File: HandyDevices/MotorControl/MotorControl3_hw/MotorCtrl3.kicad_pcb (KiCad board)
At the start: 2 copper layers, 90 x 108 mm, 202 parts, among them Q1 USBLC6_2XX, Q2 MMBT2222, Q3 LED_RGB, SW1 BUTTON, SW2 BUTTON, U1 L6470, U2 L6470, U3 L6470, U4 L6470

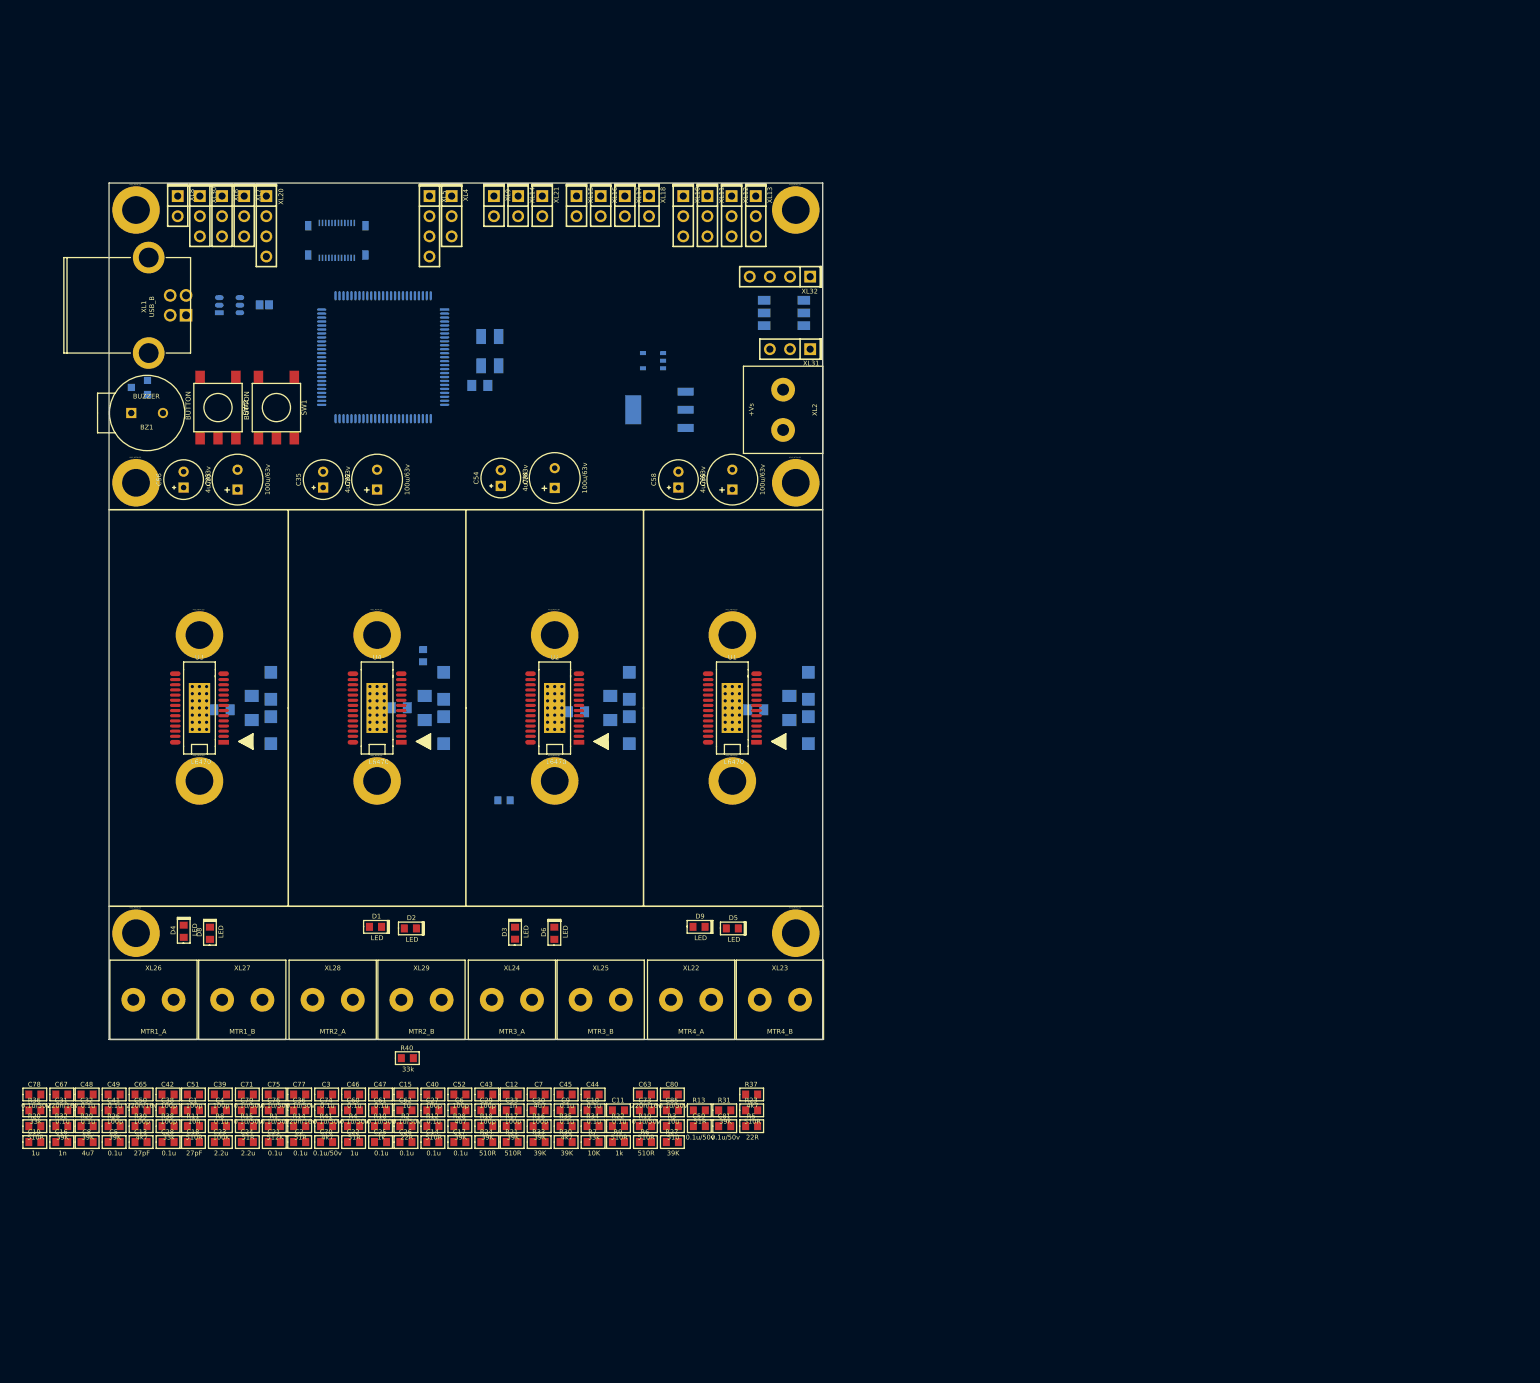
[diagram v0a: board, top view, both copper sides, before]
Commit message: MotorControl3 Footprint aligned.
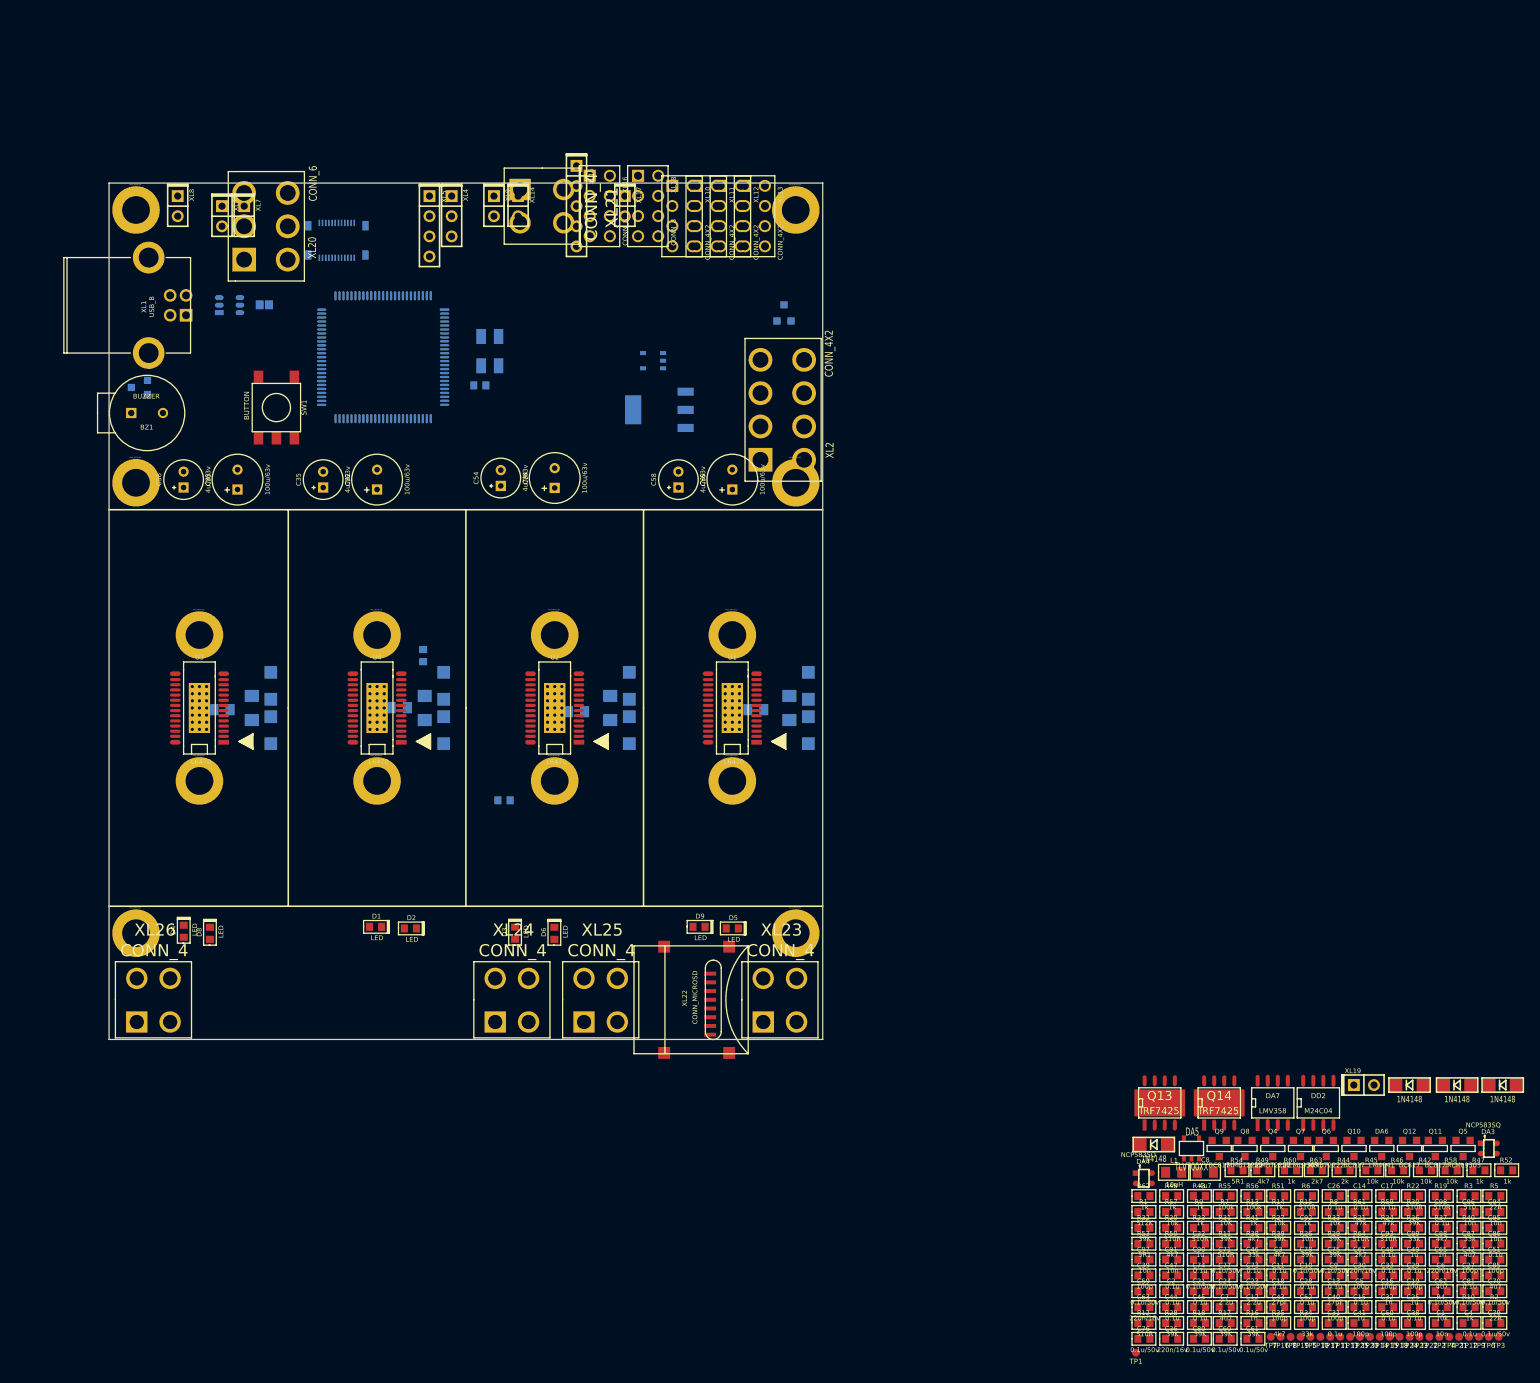
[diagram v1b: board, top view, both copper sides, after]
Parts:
- removed SW2: BUTTON, BUTTON_6x6SMD
- removed XL27: MTR1_B, CONN_KF128D_2
- removed XL28: MTR2_A, CONN_KF128D_2
- removed XL29: MTR2_B, CONN_KF128D_2
- removed XL30, XL31: CONN_3, CONN_PLS-3
- removed XL32: CONN_4, CONN_PLS-4
- added C86: 0.1u, CAP_0603, F.Cu at (350.8, 220.8)
- added C87: 4u7, CAP_0603, F.Cu at (347.5, 220.8)
- added C88: 1n, CAP_0603, F.Cu at (344.0, 220.8)
- added C89: 1u, CAP_0603, F.Cu at (340.5, 220.8)
- added C90: 0.1u, CAP_0603, F.Cu at (313.5, 222.8)
- added C91: 10n, CAP_0603, F.Cu at (310.0, 222.8)
- added C92: 10n, CAP_0603, F.Cu at (327.0, 218.8)
- added C93: 0.1u, CAP_0603, F.Cu at (337.2, 220.8)
- added C94: 10n, CAP_0603, F.Cu at (350.8, 216.8)
- added C95: 10n, CAP_0603, F.Cu at (350.8, 218.8)
- added C96: 10n, CAP_0603, F.Cu at (347.5, 216.8)
- added C97: 10n, CAP_0603, F.Cu at (306.5, 222.8)
- added C98: 0.1u, CAP_0603, F.Cu at (344.0, 216.8)
- added D17: 1N4148, DIODE_SOD80C, F.Cu at (340.0, 200.8)
- added D18: 1N4148, DIODE_SOD80C, F.Cu at (351.8, 200.8)
- added D19: 1N4148, DIODE_SOD80C, F.Cu at (307.8, 208.2)
- added D20: 1N4148, DIODE_SOD80C, F.Cu at (346.0, 200.8)
- added DA3: NCP583SQ, SC82AB, F.Cu at (350.0, 208.8)
- added DA4: NCP583SQ, SC82AB, F.Cu at (306.5, 212.5)
- added DA5: TLV700XX, SOT23-5, F.Cu at (312.5, 208.8)
- added DA6: LM4041, SOT23, F.Cu at (336.5, 208.8)
- added DA7: LMV358, SO8E, F.Cu at (322.8, 203.0)
- added DD2: M24C04, SO8E, F.Cu at (328.5, 203.0)
- added L1: 10uH, IND_0805, F.Cu at (310.2, 211.8)
- added Q10: BC817, SOT23, F.Cu at (333.0, 208.8)
- added Q11: BC817, SOT23, F.Cu at (343.2, 208.8)
- added Q12: BC817, SOT23, F.Cu at (340.0, 208.8)
- added Q13: IRF7425, SO8HEATSINK, F.Cu at (308.5, 203.0)
- added Q14: IRF7425, SO8HEATSINK, F.Cu at (316.0, 203.0)
- added Q4: MMBT2222, SOT23, F.Cu at (322.8, 208.8)
- added Q5: IRLML9303, SOT23, F.Cu at (346.8, 208.8)
- added Q6: MMBT2222, SOT23, F.Cu at (329.5, 208.8)
- added Q7: IRLML9303, SOT23, F.Cu at (326.2, 208.8)
- added Q8: MMBT2222, SOT23, F.Cu at (319.2, 208.8)
- added Q9: BC817, SOT23, F.Cu at (316.0, 208.8)
- added R42: 10k, RES_0603, F.Cu at (342.0, 211.5)
- added R43: 1k, RES_0603, F.Cu at (313.5, 214.8)
- added R44: 2k, RES_0603, F.Cu at (331.8, 211.5)
- added R45: 10k, RES_0603, F.Cu at (335.2, 211.5)
- added R46: 10k, RES_0603, F.Cu at (338.5, 211.5)
- added R47: 1k, RES_0603, F.Cu at (348.8, 211.5)
- added R48: 1k, RES_0603, F.Cu at (310.0, 214.8)
- added R49: 4k7, RES_0603, F.Cu at (321.5, 211.5)
- added R50: 4k7, RES_0603, F.Cu at (310.0, 220.8)
- added R51: 1k, RES_0603, F.Cu at (323.5, 214.8)
- added R52: 1k, RES_0603, F.Cu at (352.2, 211.5)
- added R53: 5R1, RES_0603, F.Cu at (306.5, 220.8)
- added R54: 5R1, RES_0603, F.Cu at (318.2, 211.5)
- added R55: 100k, RES_0603, F.Cu at (316.8, 214.8)
- added R56: 100k, RES_0603, F.Cu at (320.2, 214.8)
- added R57: 10k, RES_0603, F.Cu at (310.0, 216.8)
- added R58: 10k, RES_0603, F.Cu at (345.2, 211.5)
- added R59: 47k, RES_0603, F.Cu at (337.2, 216.8)
- added R60: 1k, RES_0603, F.Cu at (325.0, 211.5)
- added R61: 47k, RES_0603, F.Cu at (333.8, 216.8)
- added R62: 1k, RES_0603, F.Cu at (306.5, 214.8)
- added R63: 2k7, RES_0603, F.Cu at (328.2, 211.5)
- added R64: 2k7, RES_0603, F.Cu at (333.8, 220.8)
- added TP1: TESTPOINT, TESTPOINT_1MM, F.Cu at (305.5, 234.5)
- added TP10: TESTPOINT, TESTPOINT_1MM, F.Cu at (328.8, 232.5)
- added TP11: TESTPOINT, TESTPOINT_1MM, F.Cu at (331.2, 232.5)
- added TP12: TESTPOINT, TESTPOINT_1MM, F.Cu at (347.5, 232.5)
- added TP13: TESTPOINT, TESTPOINT_1MM, F.Cu at (332.5, 232.5)
- added TP14: TESTPOINT, TESTPOINT_1MM, F.Cu at (336.2, 232.5)
- added TP15: TESTPOINT, TESTPOINT_1MM, F.Cu at (337.5, 232.5)
- added TP16: TESTPOINT, TESTPOINT_1MM, F.Cu at (323.8, 232.5)
- added TP17: TESTPOINT, TESTPOINT_1MM, F.Cu at (330.0, 232.5)
- added TP18: TESTPOINT, TESTPOINT_1MM, F.Cu at (338.8, 232.5)
- added TP19: TESTPOINT, TESTPOINT_1MM, F.Cu at (326.2, 232.5)
- added TP2: TESTPOINT, TESTPOINT_1MM, F.Cu at (343.8, 232.5)
- added TP20: TESTPOINT, TESTPOINT_1MM, F.Cu at (335.0, 232.5)
- added TP21: TESTPOINT, TESTPOINT_1MM, F.Cu at (346.2, 232.5)
- added TP22: TESTPOINT, TESTPOINT_1MM, F.Cu at (342.5, 232.5)
- added TP23: TESTPOINT, TESTPOINT_1MM, F.Cu at (341.2, 232.5)
- added TP24: TESTPOINT, TESTPOINT_1MM, F.Cu at (340.0, 232.5)
- added TP25: TESTPOINT, TESTPOINT_1MM, F.Cu at (333.8, 232.5)
- added TP3: TESTPOINT, TESTPOINT_1MM, F.Cu at (351.2, 232.5)
- added TP4: TESTPOINT, TESTPOINT_1MM, F.Cu at (345.0, 232.5)
- added TP5: TESTPOINT, TESTPOINT_1MM, F.Cu at (327.5, 232.5)
- added TP6: TESTPOINT, TESTPOINT_1MM, F.Cu at (350.0, 232.5)
- added TP7: TESTPOINT, TESTPOINT_1MM, F.Cu at (322.5, 232.5)
- added TP8: TESTPOINT, TESTPOINT_1MM, F.Cu at (325.0, 232.5)
- added TP9: TESTPOINT, TESTPOINT_1MM, F.Cu at (348.8, 232.5)
- added XL19: CONN_2, CONN_PLS-2, F.Cu at (334.2, 200.8)
- C20: value 10u -> 4u7; footprint CAP_0805 -> CAP_0603
- C8: footprint CAP_0603 -> CAP_0805
- C85: value 10u -> 4u7
- Q3: value LED_RGB -> IRLML9303; footprint LED_HH5050_RGB -> SOT23
- R13, R15: value 51R -> 1k
- R14, R4: value 51R -> 10k
- R8: value 100K -> 10k
- XL10, XL11, XL12, XL13: value CONN_3 -> CONN_4X2; footprint CONN_PLS-3 -> CONN_DIL2X4
- XL15: value CONN_2 -> CONN_5; footprint CONN_PLS-2 -> CONN_PLS-5
- XL16, XL18: value CONN_2 -> CONN_8; footprint CONN_PLS-2 -> CONN_DIL2X4
- XL2: value +Vs -> CONN_4X2; footprint CONN_KF128D_2 -> MINIFIT_8
- XL20: value CONN_4 -> CONN_6; footprint CONN_PLS-4 -> MINIFIT_6
- XL21: value CONN_2 -> CONN_4; footprint CONN_PLS-2 -> MINIFIT_4
- XL22: value MTR4_A -> CONN_MICROSD; footprint CONN_KF128D_2 -> MICROSD_CAP_FIX05A
- XL23: value MTR4_B -> CONN_4; footprint CONN_KF128D_2 -> MINIFIT_4
- XL24: value MTR3_A -> CONN_4; footprint CONN_KF128D_2 -> MINIFIT_4
- XL25: value MTR3_B -> CONN_4; footprint CONN_KF128D_2 -> MINIFIT_4
- XL26: value MTR1_A -> CONN_4; footprint CONN_KF128D_2 -> MINIFIT_4
- XL6, XL7: value CONN_3 -> CONN_2; footprint CONN_PLS-3 -> CONN_PLS-2
- moved C19 174.9 mm to (340.5, 226.8)
- moved R36 174.5 mm to (340.5, 218.8)
- moved C16 168.3 mm to (337.2, 226.8)
- moved C32 165.9 mm to (337.2, 228.8)
- moved C51 165.4 mm to (350.8, 222.8)
- moved C42 165.4 mm to (347.5, 222.8)
- moved C48 165.3 mm to (337.2, 222.8)
- moved C65 165.3 mm to (344.0, 222.8)
- moved C49 165.2 mm to (340.5, 222.8)
- moved C67 165.0 mm to (333.8, 222.8)
- moved C31 162.7 mm to (330.5, 230.8)
- moved C78 161.7 mm to (327.0, 222.8)
- moved C4 159.7 mm to (347.5, 230.8)
- moved C1 159.6 mm to (344.0, 230.8)
- moved C79 159.6 mm to (350.8, 230.8)
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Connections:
- BZ1 pad 2: +3.3V -> +5V
- C21 pad 1: +3.3V -> VAA
- C22 pad 1: +3.3V -> VAA
- C25 pad 1: N-00000151 -> /URef
- C28 pad 1: /NRST -> /STBY/RST
- C33 pad 1: /STBY/RST_4 -> /STBY/RST
- C50 pad 1: /STBY/RST_3 -> /STBY/RST
- C51 pad 1: /STBY/RST_1 -> /STBY/RST
- C52 pad 1: /STBY/RST_2 -> /STBY/RST
- C85 pad 1: +3.3V -> +5V
- DD1 pad 14: /NRST -> /STBY/RST
- DD1 pad 15: /LIMITER1 -> /HEAD_ADC
- DD1 pad 16: /LIMITER2 -> /BED_ADC
- DD1 pad 17: /LIMITER3 -> /LIMITER1
- DD1 pad 18: /LIMITER4 -> /LIMITER3
- DD1 pad 21: N-00000151 -> /URef
- DD1 pad 22: +3.3V -> VAA
- DD1 pad 23: /PA0 -> /LCD_BCKLT
- DD1 pad 25: /TX2 -> /ENCODER1
- DD1 pad 26: /RX2 -> /ENCODER2
- DD1 pad 29: /DAC1 -> /BUTTON
- DD1 pad 33: /OPT_LIMITER1 -> /LIMITER5
- DD1 pad 34: (no net) -> /LIMITER7
- DD1 pad 37: /Vacuum3 -> /GPIO1
- DD1 pad 47: /TX3 -> /Fan
- DD1 pad 48: /RX3 -> /GPIO4
- DD1 pad 51: (no net) -> /GPIO5
- DD1 pad 52: /SPI2_SCK -> /GPIO6
- DD1 pad 53: /SPI2_MISO -> /HEAD_HEATER
- DD1 pad 54: /SPI2_MOSI -> /BED_HEATER
- DD1 pad 55: /STBY/RST_3 -> /SW_3
- DD1 pad 56: /BUSY/SYNC_3 -> /FLAG_3
- DD1 pad 57: /FLAG_3 -> /BUSY/SYNC_4
- DD1 pad 58: /SW_3 -> /SW_4
- DD1 pad 59: /STBY/RST_4 -> /FLAG_4
- DD1 pad 60: /BUSY/SYNC_4 -> /LIMITER6
- DD1 pad 62: /FLAG_4 -> /LIMITER8
- DD1 pad 63: /LED_RED -> /Buzzer
- DD1 pad 64: /LED_GREEN -> /LIMITER2
- DD1 pad 65: /LED_BLUE -> /SD_DAT0
- DD1 pad 66: /PC9 -> /SD_DAT1
- DD1 pad 69: (no net) -> /GPIO7
- DD1 pad 7: /SW_4 -> (no net)
- DD1 pad 77: (no net) -> /LIMITER4
- DD1 pad 78: /OPT_LIMITER2 -> /SD_DAT2
- DD1 pad 79: /OPT_LIMITER3 -> /SD_DAT3
- DD1 pad 80: /OPT_LIMITER4 -> /SD_CLK
- DD1 pad 81: /STBY/RST_1 -> /BUSY/SYNC_1
- DD1 pad 82: /BUSY/SYNC_1 -> /SW_1
- DD1 pad 83: /FLAG_1 -> /SD_CMD
- DD1 pad 84: /SW_1 -> /FLAG_1
- DD1 pad 85: /STBY/RST_2 -> /BUSY/SYNC_2
- DD1 pad 86: /BUSY/SYNC_2 -> /SW_2
- DD1 pad 88: /SW_2 -> /BUSY/SYNC_3
- DD1 pad 89: (no net) -> /GPIO2
- DD1 pad 91: (no net) -> /GPIO3
- DD1 pad 95: /Buzzer -> /I2C_SCL
- DD1 pad 96: /LCD_BCKLT -> /I2C_SDA
- R13 pad 1: /LED_RED -> N-00000113
- R13 pad 2: N-0000096 -> /Fan
- R14 pad 1: /LED_GREEN -> +12V
- R14 pad 2: N-0000095 -> N-00000110
- R15 pad 1: /LED_BLUE -> N-00000111
- R15 pad 2: N-0000094 -> /Vacuum1
- R18 pad 2: /STBY/RST_4 -> /STBY/RST
- R31 pad 2: /STBY/RST_3 -> /STBY/RST
- R32 pad 2: /STBY/RST_1 -> /STBY/RST
- R33 pad 2: /STBY/RST_2 -> /STBY/RST
- R4 pad 1: N-00000151 -> +12V
- R4 pad 2: +3.3V -> N-00000123
- R8 pad 2: /NRST -> /STBY/RST
- U1 pad 3: /STBY/RST_4 -> /STBY/RST
- U2 pad 3: /STBY/RST_3 -> /STBY/RST
- U3 pad 3: /STBY/RST_1 -> /STBY/RST
- U4 pad 3: /STBY/RST_2 -> /STBY/RST
- XL10 pad 1: +5V -> (no net)
- XL10 pad 2: /OPT_LIMITER1 -> (no net)
- XL10 pad 3: GND -> +5V
- XL11 pad 1: +5V -> (no net)
- XL11 pad 2: /OPT_LIMITER2 -> (no net)
- XL11 pad 3: GND -> +5V
- XL12 pad 1: +5V -> (no net)
- XL12 pad 2: /OPT_LIMITER3 -> (no net)
- XL12 pad 3: GND -> +5V
- XL13 pad 1: +5V -> (no net)
- XL13 pad 2: /OPT_LIMITER4 -> (no net)
- XL13 pad 3: GND -> +5V
- XL14 pad 1: /Vacuum2 -> /Vac1_Out
- XL15 pad 1: /LIMITER1 -> GND
- XL15 pad 2: GND -> /ENCODER1
- XL16 pad 1: /LIMITER2 -> +12V
- XL16 pad 2: GND -> +12V
- XL17 pad 1: /LIMITER3 -> /Vac2_Out
- XL18 pad 1: /LIMITER4 -> /GPIO1
- XL18 pad 2: GND -> /GPIO2
- XL20 pad 1: /SPI2_SCK -> /BED_HEATER_OUT
- XL20 pad 2: /SPI2_MISO -> /BED_HEATER_OUT
- XL20 pad 3: /SPI2_MOSI -> /BED_R
- XL20 pad 4: GND -> AGND
- XL21 pad 1: /Vacuum3 -> /HEAD_HEATER_OUT
- XL21 pad 2: GND -> /HEAD_R
- XL22 pad 1: /OUT4_1A -> /SD_DAT2
- XL22 pad 2: /OUT4_2A -> /SD_DAT3
- XL23 pad 1: /OUT4_1B -> /OUT3_1A
- XL23 pad 2: /OUT4_2B -> /OUT3_2A
- XL24 pad 1: /OUT3_1A -> /OUT1_1A
- XL24 pad 2: /OUT3_2A -> /OUT1_2A
- XL25 pad 1: /OUT3_1B -> /OUT4_1A
- XL25 pad 2: /OUT3_2B -> /OUT4_2A
- XL26 pad 1: /OUT1_1A -> /OUT2_1A
- XL26 pad 2: /OUT1_2A -> /OUT2_2A
- XL6 pad 1: GND -> +12V
- XL6 pad 2: /TX2 -> GND
- XL7 pad 1: GND -> +12V
- XL7 pad 2: /TX3 -> GND
- XL8 pad 1: GND -> +12V
- XL8 pad 2: /DAC1 -> GND
- XL9 pad 1: /Vacuum1 -> /Fan_Out

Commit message: MotorCtrl3 start to trace board.
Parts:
- C20, C34, C37, C53, C55, C57, C64, C66, C68, C72, D10, D11, D12, D13, D14, D15, D16, D7, DA1, DA2, DD1, F1, Q1, Q2, Q3, R25, XL3, XTAL1: moved to F.Cu
- moved C85 201.8 mm to (184.8, 109.9)
- moved R10 198.8 mm to (188.1, 109.9)
- moved C86 194.7 mm to (196.4, 102.2), turned to 90 degrees
- moved C87 193.3 mm to (194.8, 102.2), turned to 90 degrees
- moved C4 191.3 mm to (208.7, 99.2), turned to 270 degrees
- moved C88 189.7 mm to (192.0, 107.2), turned to 90 degrees
- moved C89 188.7 mm to (189.8, 107.2), turned to 90 degrees
- moved C5 187.5 mm to (196.4, 99.2), turned to 270 degrees
- moved C19 182.5 mm to (207.1, 102.2), turned to 90 degrees
- moved C16 182.3 mm to (207.1, 99.2), turned to 270 degrees
- moved C6 179.4 mm to (224.2, 91.2), turned to 90 degrees
- moved DA3 175.4 mm to (208.1, 105.8), turned to 270 degrees
- moved C15 174.1 mm to (206.3, 110.2), turned to 180 degrees
- moved R44 171.7 mm to (192.8, 110.6)
- moved C27 168.9 mm to (218.4, 115.8)
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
